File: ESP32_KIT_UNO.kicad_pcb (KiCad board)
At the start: 2 copper layers, 69.1 x 53.8 mm, 55 parts, among them Q1 BC817, Q2 BC817, U1 ESP32-WROOM-32, U2 CH340C, U3 AMS1117-3.3, U5 MP1482DS-LF-Z, U6 LMV321

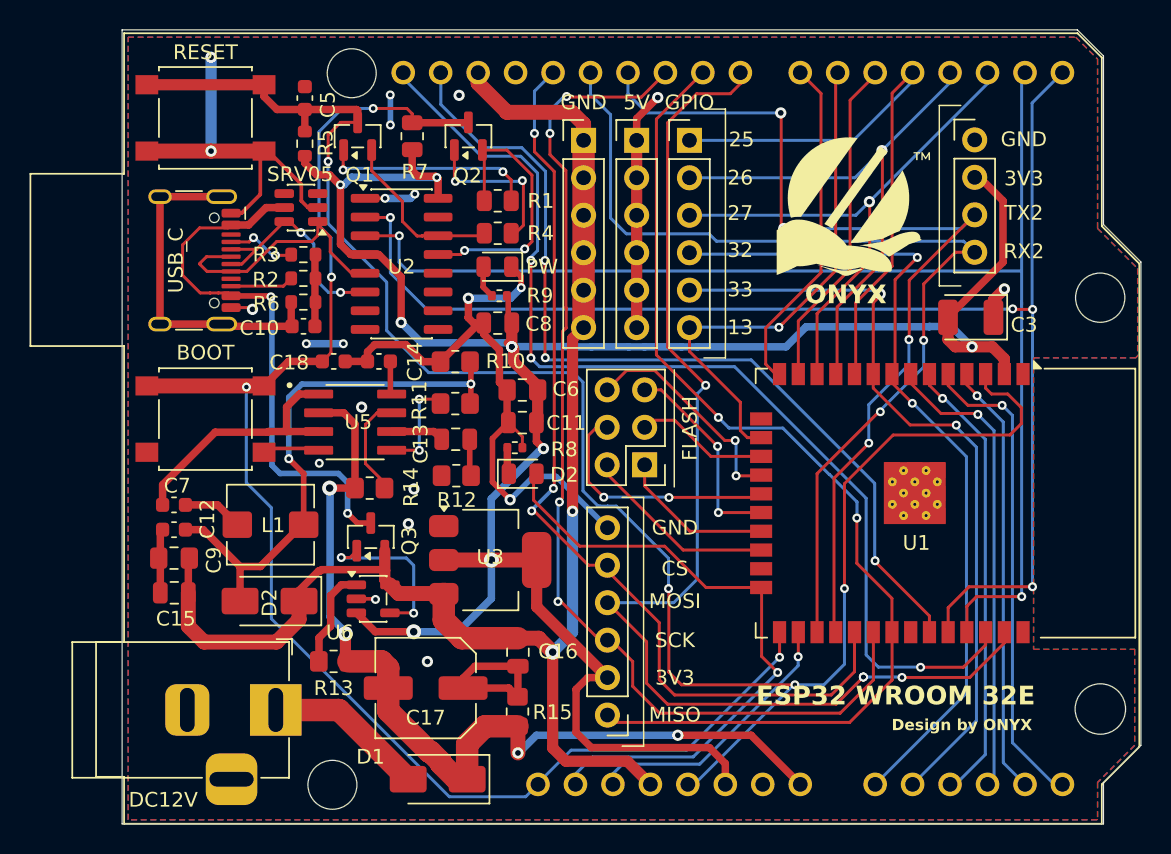
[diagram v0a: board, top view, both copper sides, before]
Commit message: Cap nhat file thiet ke KiCad va xuat file Gerber PDF
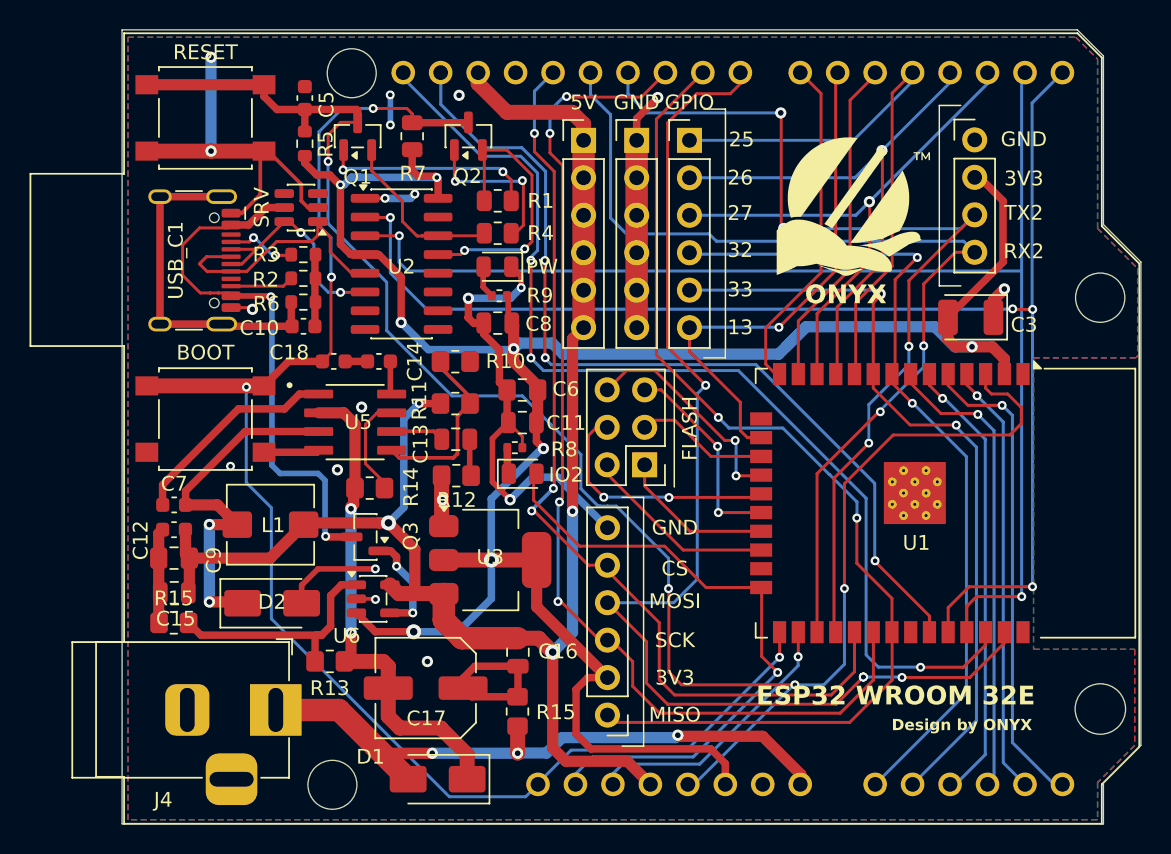
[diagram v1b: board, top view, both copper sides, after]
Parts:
- added R15: 100k, Resistor_SMD:R_0805_2012Metric_Pad1.20x1.40mm_HandSolder, F.Cu at (139.5, 106.9)
- C11: value 100nF -> 0.1uF
- C12: value 10nF -> 22uF
- C6: value 0.1uF -> 22uF
- J4: renamed from DC12V; value (none) -> Jack DC
- R12: value 2k2 -> 5k6
- R13: value 220k -> 100k
- moved Q3 0.36 mm to (152.5, 101.1), turned to 180 degrees
- moved R13 0.26 mm to (150.1, 109.5)
- moved D2 0.23 mm to (146.2, 105.6), turned to 0 degrees
- turned C7 to 0 degrees
- turned C12 to 180 degrees
- renumbered GND to 5V, 5V to GND, D2 to IO2, SPI to SPI1, SRV05 to SRV, USB_C to USB_C1
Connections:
- C12 pad 1: GND -> /+5V
- C12 pad 2: Net-(D2-A) -> GND
- C17 pad 2: /VIN -> Net-(D1-K)
- C7 pad 1: Net-(C7-Pad1) -> Net-(U5-BS)
- C7 pad 2: Net-(U5-BS) -> Net-(D2-K)
- D1 pad 1: /VIN -> Net-(D1-K)
- D1 pad 2: Net-(D1-A) -> /VIN
- D2 pad 1: /+5V -> Net-(D2-K)
- D2 pad 2: Net-(D2-A) -> GND
- J4 pad 1: Net-(D1-A) -> /VIN
- L1 pad 1: Net-(C7-Pad1) -> Net-(D2-K)
- L1 pad 2: Net-(D2-A) -> /+5V
- R10 pad 1: Net-(D2-A) -> GND
- R10 pad 2: GND -> Net-(U5-FB)
- R11 pad 1: Net-(U5-FB) -> /+5V
- R11 pad 2: Net-(D2-A) -> Net-(U5-FB)
- R13 pad 2: /VIN -> Net-(D1-K)
- R14 pad 1: /VIN -> Net-(D1-K)
- U5 pad 2: /VIN -> Net-(D1-K)
- U5 pad 3: Net-(U5-BS) -> Net-(D2-K)
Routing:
- net Net-(D2-A): track 36.6 -> 0.00 mm, vias 2 -> 0
- net Net-(D1-K): track 0.00 -> 33.4 mm, vias 0 -> 2
- net Net-(D2-K): track 0.00 -> 25.6 mm, vias 0 -> 2
- net /VIN: track 63.4 -> 44.1 mm, vias 4 -> 3
- net Net-(D1-A): track 10.9 -> 0.00 mm
- net /+5V: track 97.9 -> 107.9 mm, vias 2 -> 4
- net Net-(U6-+): track 6.84 -> 16.5 mm
- net Net-(U5-FB): track 6.85 -> 11.8 mm, vias 2 -> 0
- net Net-(AO3401A1-G): track 11.2 -> 7.15 mm
- net Net-(C7-Pad1): track 4.07 -> 0.00 mm
- net Net-(U5-BS): track 17.6 -> 14.5 mm
- net +3.3V: track 155.4 -> 158.5 mm, vias 9 -> 8
- net /EN: track 126.7 -> 123.7 mm
- net GND: track 123.0 -> 123.1 mm, vias 21 -> 20
